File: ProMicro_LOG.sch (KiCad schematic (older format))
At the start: 17 parts, among them J1 Micro_SD_Card_Det, U1 DS3231MZ

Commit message: kicad-exports
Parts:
- removed TP2: initials, Symbol:initials, symbol Connector:TestPoint_Small
- added TP2: TestPoint, symbol Connector:TestPoint
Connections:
- net D6: no longer JP1.2
- net D8: now also JP1.2
- net at JP2.2: now also TP2.1
- net A0: no longer names the net of A1.17 (A0)
- net A1: no longer names the net of A1.18 (A1)
- net A2: no longer names the net of A1.19 (A2)
- net A3: no longer names the net of A1.20 (A3)
- net D0: no longer names the net of A1.2 (D0/RX)
- net D1: no longer names the net of A1.1 (D1/TX)
- net D4: no longer names the net of A1.7 (D4)
- net D5: no longer names the net of A1.8 (D5)
- net D7: no longer names the net of A1.10 (D7)
- no-connect marks 1 -> 13
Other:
- note added: "INT"
- note added: "SDI"
- note added: "SDO"
- note removed: "MISO"
- note removed: "MOSI"
- note removed: "what the hell\nhappened here!!!"
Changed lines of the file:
@@
 encoding utf-8
 Sheet 1 1
-Title "https://github.com/nerdyscout/ProMicro_LOG"
+Title "ProMicro_LOG"
 Date "2020-07-13"
 Rev "v1.0"
@@
 	10000 5650 10000 5810
 Wire Wire Line
-	8200 2400 8400 2400
-Wire Wire Line
-	8200 2500 8400 2500
-Wire Wire Line
 	8200 2600 8400 2600
 Wire Wire Line
 	8200 2700 8400 2700
 Wire Wire Line
-	8200 2800 8400 2800
-Wire Wire Line
-	8200 2900 8400 2900
-Wire Wire Line
 	8200 3000 8400 3000
 Wire Wire Line
-	8200 3100 8400 3100
-Wire Wire Line
 	8200 3200 8400 3200
 Wire Wire Line
@@
 Wire Wire Line
 	9400 2400 9600 2400
-Wire Wire Line
-	9400 3000 9600 3000
-Wire Wire Line
-	9400 3100 9600 3100
-Wire Wire Line
-	9400 3200 9600 3200
-Wire Wire Line
-	9400 3300 9600 3300
 Text Notes 7900 2830 2    50   ~ 0
 VBAT/2
@@
 Text Notes 9800 3330 0    50   ~ 0
 TCK
-Text GLabel 8200 2400 0    50   Input ~ 0
-D0
-Text GLabel 8200 2500 0    50   Output ~ 0
-D1
 Text GLabel 8200 2600 0    50   BiDi ~ 0
 D2
 Text GLabel 8200 2700 0    50   Output ~ 0
 D3
-Text GLabel 8200 2800 0    50   Input ~ 0
-D4
-Text GLabel 8200 2900 0    50   BiDi ~ 0
-D5
 Text GLabel 8200 3000 0    50   BiDi ~ 0
 D6
-Text GLabel 8200 3100 0    50   BiDi ~ 0
-D7
 Text GLabel 8200 3200 0    50   BiDi ~ 0
 D8
@@
 Text GLabel 9600 2400 2    50   Input ~ 0
 Reset
-Text GLabel 9600 3000 2    50   Input ~ 0
-A0
-Text GLabel 9600 3100 2    50   Input ~ 0
-A1
-Text GLabel 9600 3200 2    50   Input ~ 0
-A2
-Text GLabel 9600 3300 2    50   Input ~ 0
-A3
 $Comp
 L power:+3V3 #PWR0102
@@
 SCL
 Text Notes 7900 3525 2    50   ~ 0
-MOSI
+SDO
 Text Notes 7900 3625 2    50   ~ 0
-MISO
+SDI
 Text Notes 7900 3725 2    50   ~ 0
 SCK
@@
 $EndComp
 Text GLabel 6750 5100 2    50   BiDi ~ 0
-D6
+D8
 Wire Wire Line
 	6750 5100 6600 5100
@@
 BTN
 $Comp
-L Connector:TestPoint_Small TP2
-U 1 1 5EDCB516
-P 10500 6250
-F 0 "TP2" H 10550 6300 50  0001 L CNN
-F 1 "initials" H 10550 6250 50  0000 L CNN
-F 2 "Symbol:initials" H 10700 6250 50  0001 C CNN
-F 3 "~" H 10700 6250 50  0001 C CNN
-	1    10500 6250
-	1    0    0    -1
-$EndComp
-$Comp
 L MCU_Module:Sparkfun_Pro_Micro_3V3 A1
 U 1 1 5EDCCCBD
@@
 	1    0    0    -1
 $EndComp
-Text Notes 6650 4850 0    50   ~ 0
-what the hell\nhappened here!!!
+Text Notes 7900 3225 2    50   ~ 0
+INT
+$Comp
+L Connector:TestPoint TP2
+U 1 1 5F1740AB
+P 6750 4800
+F 0 "TP2" V 6675 5000 50  0000 L CNN
+F 1 "TestPoint" V 6775 5000 50  0000 L CNN
+F 2 "" H 6950 4800 50  0001 C CNN
+F 3 "~" H 6950 4800 50  0001 C CNN
+	1    6750 4800
+	0    1    1    0
+$EndComp
+Wire Wire Line
+	6600 4800 6750 4800
+NoConn ~ 8400 3100
+NoConn ~ 8400 2900
+NoConn ~ 8400 2800
+NoConn ~ 8400 2500
+NoConn ~ 8400 2400
+NoConn ~ 8800 2000
+NoConn ~ 9400 3300
+NoConn ~ 9400 3200
+NoConn ~ 9400 3100
+NoConn ~ 9400 3000
+NoConn ~ 3800 2800
+NoConn ~ 8800 4000
 $EndSCHEMATC

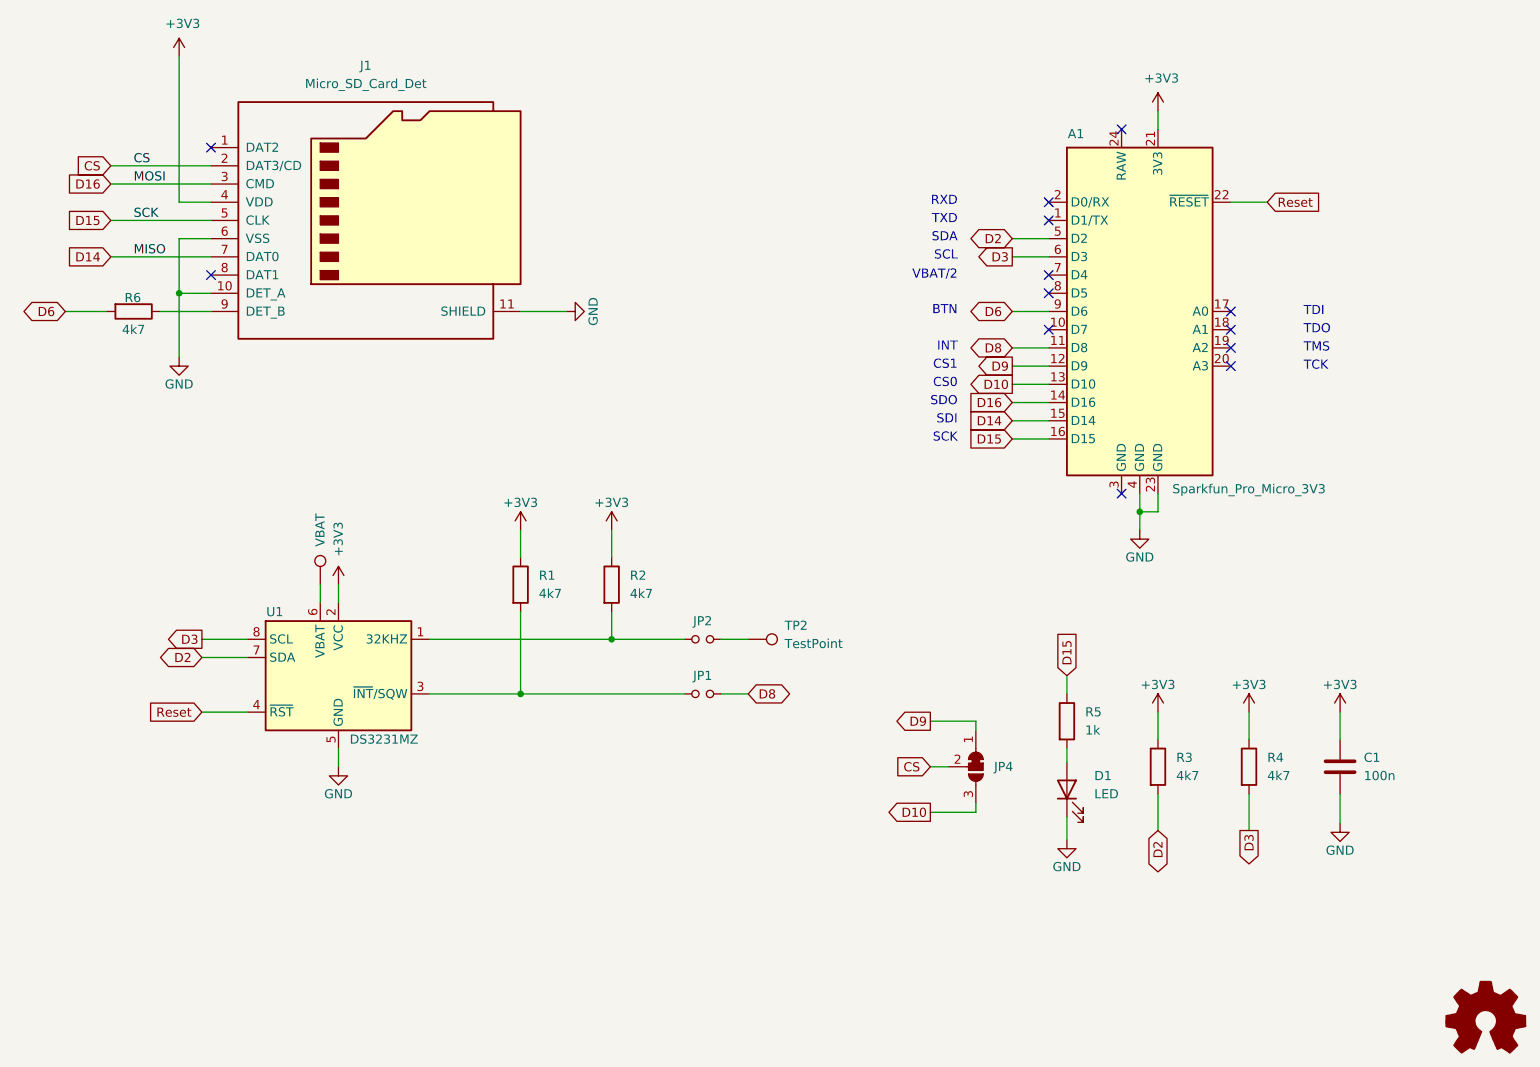
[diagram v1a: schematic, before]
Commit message: fixed missing TRG
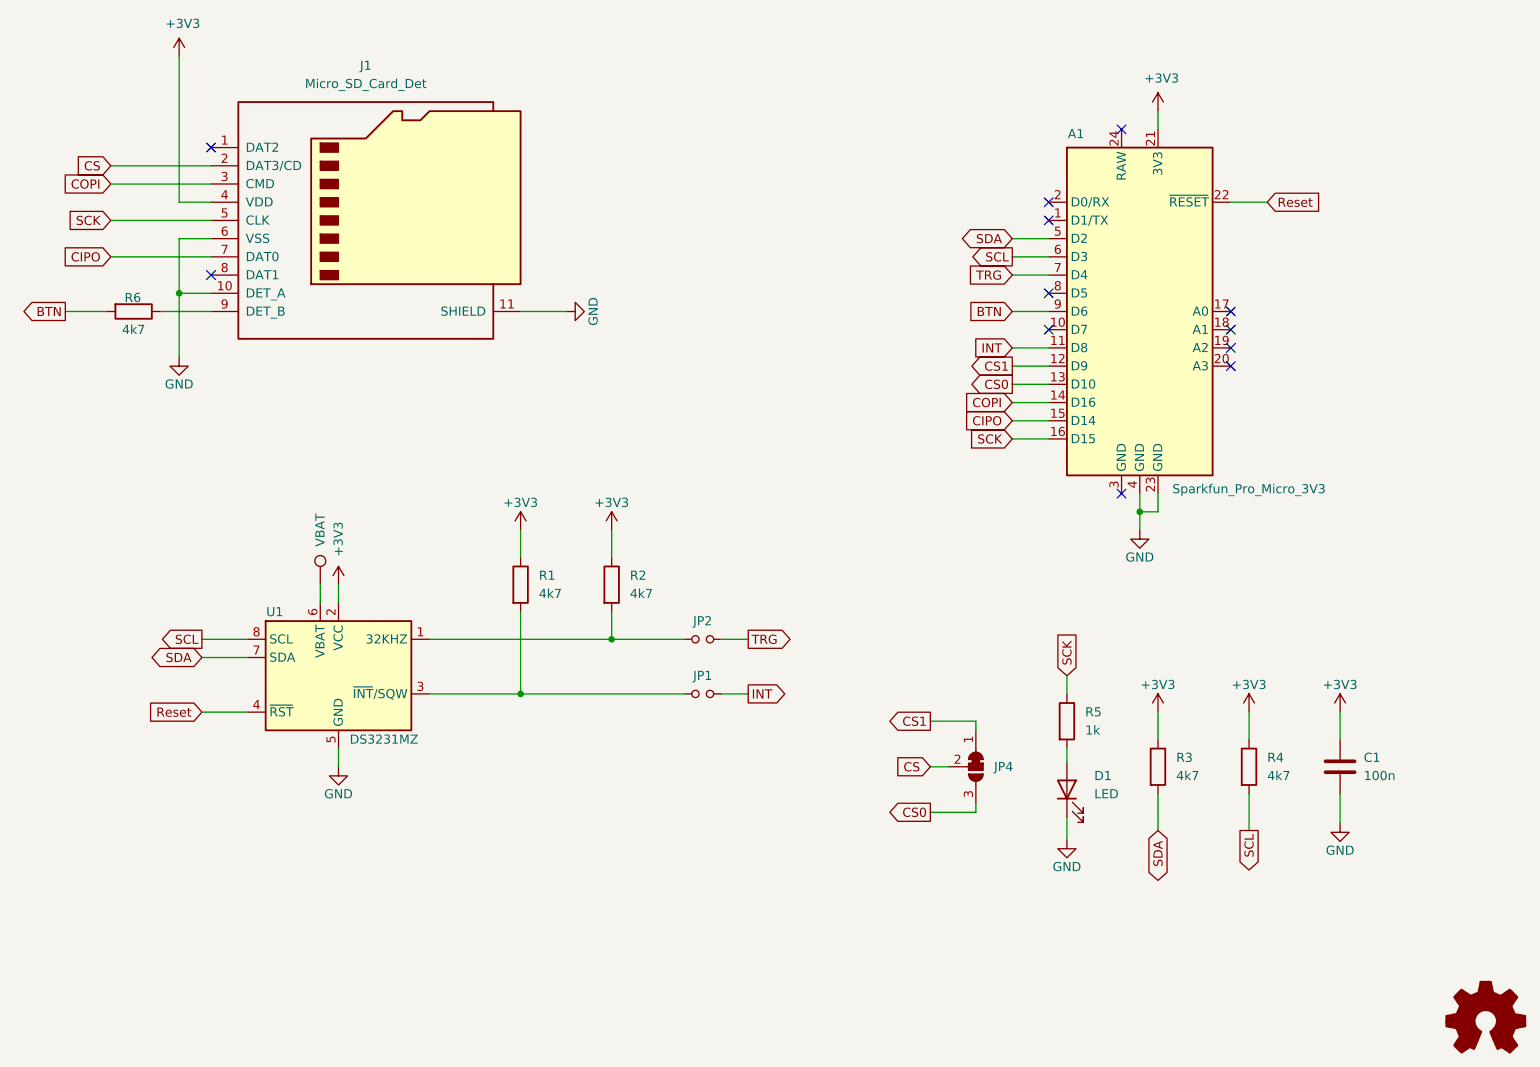
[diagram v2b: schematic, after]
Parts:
- removed TP2: TestPoint, symbol Connector:TestPoint
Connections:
- net TRG: now reaches JP2.2
- net TRG: now also A1.7 (D4)
- net D10 renamed CS0
- net D14 renamed CIPO
- net D15 renamed SCK
- net D16 renamed COPI
- net D2 renamed SDA
- net D3 renamed SCL
- net D6 renamed BTN
- net D8 renamed INT
- net D9 renamed CS1
- no-connect marks 13 -> 12
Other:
- note removed: "BTN"
- note removed: "CS0"
- note removed: "CS1"
- note removed: "INT"
- note removed: "RXD"
- note removed: "SCK"
- note removed: "SCL"
- note removed: "SDA"
- note removed: "SDI"
- note removed: "SDO"
- note removed: "TCK"
- note removed: "TDI"
- note removed: "TDO"
- note removed: "TMS"
- note removed: "TXD"
- note removed: "VBAT/2"
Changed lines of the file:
@@
 Sheet 1 1
 Title "ProMicro_LOG"
-Date "2020-07-13"
-Rev "v1.0"
+Date "2020-08-15"
+Rev "v1.1"
 Comp "https://twitter.com/nerdyscout84"
 Comment1 "CERN Open Hardware Licence v1.2"
@@
 Wire Wire Line
 	9400 2400 9600 2400
-Text Notes 7900 2830 2    50   ~ 0
-VBAT/2
-Text Notes 7900 3325 2    50   ~ 0
+Text GLabel 8200 2600 0    50   BiDi ~ 0
+SDA
+Text GLabel 8200 2700 0    50   Output ~ 0
+SCL
+Text GLabel 8200 3000 0    50   Input ~ 0
+BTN
+Text GLabel 8200 3200 0    50   Input ~ 0
+INT
+Text GLabel 8200 3300 0    50   Output ~ 0
 CS1
-Text Notes 7900 3425 2    50   ~ 0
+Text GLabel 8200 3400 0    50   Output ~ 0
 CS0
-Text Notes 9800 3030 0    50   ~ 0
-TDI
-Text Notes 9800 3130 0    50   ~ 0
-TDO
-Text Notes 9800 3230 0    50   ~ 0
-TMS
-Text Notes 9800 3330 0    50   ~ 0
-TCK
-Text GLabel 8200 2600 0    50   BiDi ~ 0
-D2
-Text GLabel 8200 2700 0    50   Output ~ 0
-D3
-Text GLabel 8200 3000 0    50   BiDi ~ 0
-D6
-Text GLabel 8200 3200 0    50   BiDi ~ 0
-D8
-Text GLabel 8200 3300 0    50   Output ~ 0
-D9
-Text GLabel 8200 3400 0    50   Output ~ 0
-D10
 Text GLabel 8200 3500 0    50   Input ~ 0
-D16
+COPI
 Text GLabel 8200 3600 0    50   Input ~ 0
-D14
+CIPO
 Text GLabel 8200 3700 0    50   Input ~ 0
-D15
+SCK
 Text GLabel 9600 2400 2    50   Input ~ 0
 Reset
@@
 	1    0    0    -1
 $EndComp
-Text Notes 7900 2425 2    50   ~ 0
-RXD
-Text Notes 7900 2525 2    50   ~ 0
-TXD
-Text Notes 7900 2625 2    50   ~ 0
-SDA
-Text Notes 7900 2725 2    50   ~ 0
-SCL
-Text Notes 7900 3525 2    50   ~ 0
-SDO
-Text Notes 7900 3625 2    50   ~ 0
-SDI
-Text Notes 7900 3725 2    50   ~ 0
-SCK
 $Comp
 L Connector:Micro_SD_Card_Det J1
@@
 	4400 4500 4400 4600
 Text GLabel 3750 4900 0    50   BiDi ~ 0
-D2
+SDA
 Text GLabel 3750 4800 0    50   Output ~ 0
-D3
+SCL
 Wire Wire Line
 	3750 4800 4000 4800
@@
 	1    0    0    -1
 $EndComp
-Text GLabel 6750 5100 2    50   BiDi ~ 0
-D8
+Text GLabel 6750 5100 2    50   Output ~ 0
+INT
 Wire Wire Line
 	6750 5100 6600 5100
@@
 	5750 3000 5500 3000
 Text GLabel 9000 5850 3    50   BiDi ~ 0
-D2
+SDA
 Text GLabel 9500 5850 3    50   Output ~ 0
-D3
+SCL
 Wire Wire Line
 	9000 5650 9000 5850
@@
 	1    0    0    -1
 $EndComp
-Text GLabel 3250 2300 0    50   Input ~ 0
-D16
 $Comp
 L power:GND #PWR0111
@@
 	3625 2600 3625 2900
 Text GLabel 3250 2700 0    50   Input ~ 0
-D14
-Text GLabel 3250 2500 0    50   Input ~ 0
-D15
+CIPO
 $Comp
 L Jumper:SolderJumper_3_Bridged12 JP4
@@
 	0    1    1    0
 $EndComp
-Text Label 3375 2500 0    50   ~ 0
-SCK
-Text Label 3375 2700 0    50   ~ 0
-MISO
-Text Label 3375 2300 0    50   ~ 0
-MOSI
-Text Label 3375 2200 0    50   ~ 0
-CS
 Text GLabel 3250 2200 0    50   Input ~ 0
 CS
@@
 	3625 2900 3625 3250
 Text GLabel 8500 5000 1    50   Input ~ 0
-D15
+SCK
 Text GLabel 7750 5250 0    50   Output ~ 0
-D9
+CS1
 Text GLabel 7750 5750 0    50   Output ~ 0
-D10
+CS0
 Wire Wire Line
 	7750 5750 8000 5750
@@
 Wire Wire Line
 	7750 5500 7850 5500
-Text GLabel 3000 3000 0    50   BiDi ~ 0
-D6
+Text GLabel 3000 3000 0    50   Output ~ 0
+BTN
 Wire Wire Line
 	3525 3000 3800 3000
@@
 	0    1    1    0
 $EndComp
-Text Notes 7900 3025 2    50   ~ 0
-BTN
 $Comp
 L MCU_Module:Sparkfun_Pro_Micro_3V3 A1
@@
 	1    0    0    -1
 $EndComp
-Text Notes 7900 3225 2    50   ~ 0
-INT
-$Comp
-L Connector:TestPoint TP2
-U 1 1 5F1740AB
-P 6750 4800
-F 0 "TP2" V 6675 5000 50  0000 L CNN
-F 1 "TestPoint" V 6775 5000 50  0000 L CNN
-F 2 "" H 6950 4800 50  0001 C CNN
-F 3 "~" H 6950 4800 50  0001 C CNN
-	1    6750 4800
-	0    1    1    0
-$EndComp
 Wire Wire Line
 	6600 4800 6750 4800
 NoConn ~ 8400 3100
 NoConn ~ 8400 2900
-NoConn ~ 8400 2800
 NoConn ~ 8400 2500
 NoConn ~ 8400 2400
@@
 NoConn ~ 3800 2800
 NoConn ~ 8800 4000
+Text GLabel 3250 2500 0    50   Input ~ 0
+SCK
+Text GLabel 3250 2300 0    50   Input ~ 0
+COPI
+Text GLabel 6750 4800 2    50   Output ~ 0
+TRG
+Text GLabel 8200 2800 0    50   Input ~ 0
+TRG
+Wire Wire Line
+	8200 2800 8400 2800
 $EndSCHEMATC
